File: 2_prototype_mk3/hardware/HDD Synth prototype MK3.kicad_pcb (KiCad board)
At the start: 2 copper layers, 119.4 x 97.4 mm, 60 parts, among them J1 Micro_SD_Card, J3 Bus_ISA_8bit, J4 Conn_01x03, J5 Conn_01x03, Q1 2N3904, SW1 SW_Push, SW2 PEC12R-2120F-S0012, U1 Optocoupler_DC_PhotoNPN_AKEC, U5 MAX98357A, U6 74LS573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

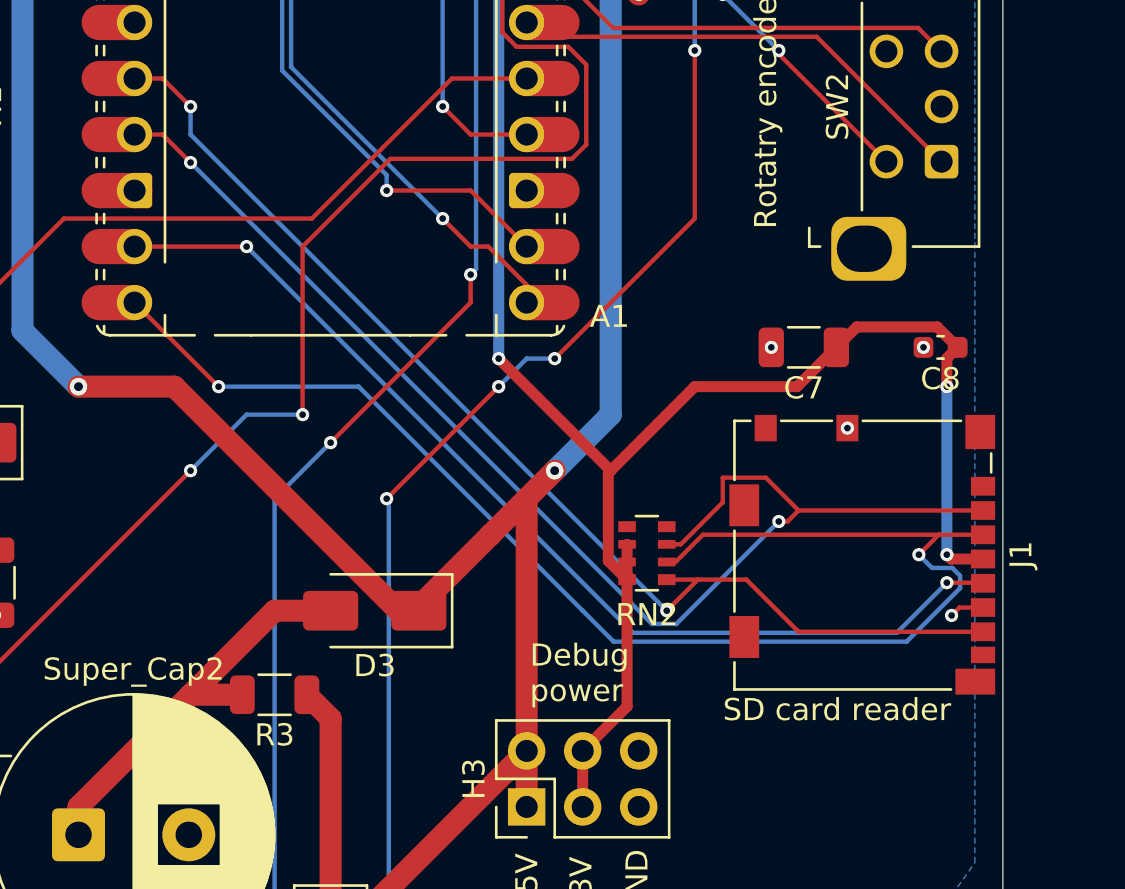
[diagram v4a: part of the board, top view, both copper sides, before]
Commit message: Switch SD card reader to better component
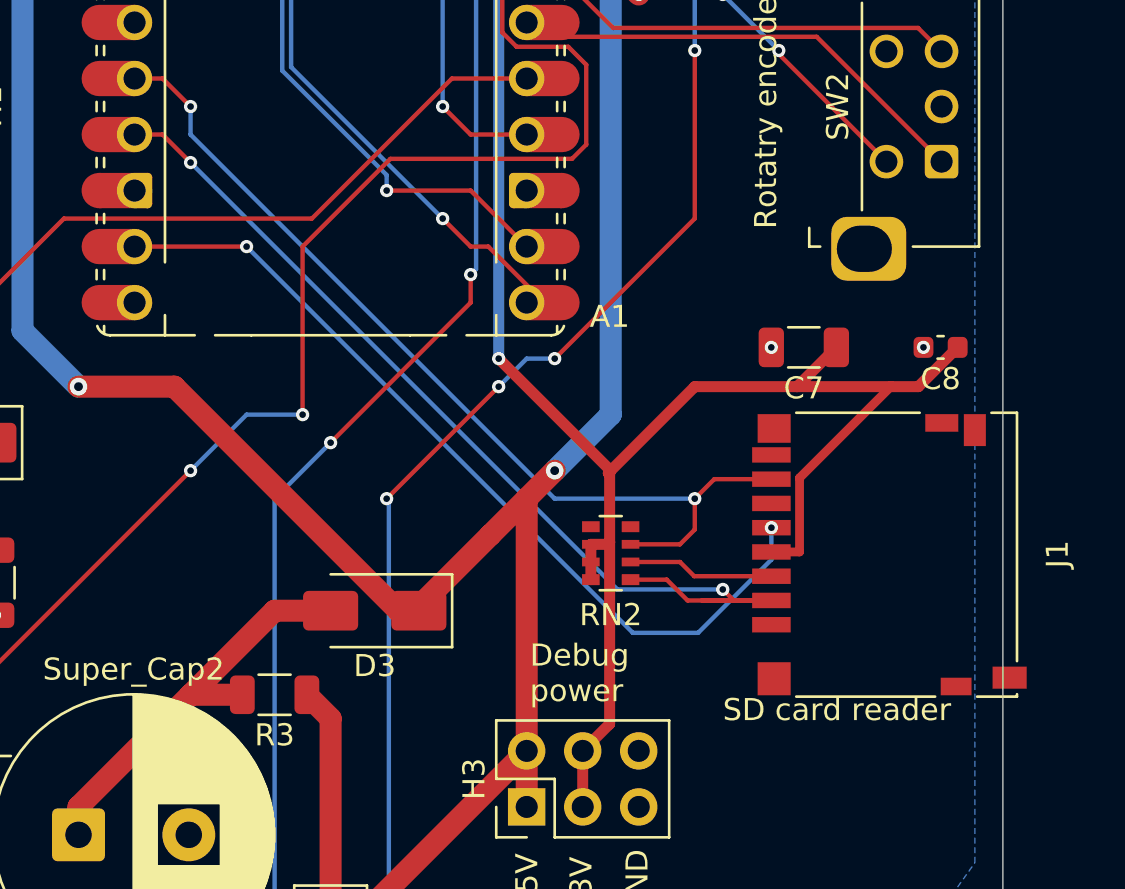
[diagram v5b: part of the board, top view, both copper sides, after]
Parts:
- A1: value RaspberryPi_Pico -> RaspberryPi_Pico2
- J1: footprint Connector_Card:microSD_HC_Molex_104031-0811 -> Connector_Card:microSD_HC_Hirose_DM3D-SF
- moved RN2 1.64 mm to (210.7, 105.3)
- moved J1 1.21 mm to (223.3, 105.4)
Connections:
- RN2 pad 1: /SD_SO -> /SD_CS
- RN2 pad 3: /SD_CS -> /SD_SO
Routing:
- net /SD_SI: track 63.8 -> 6.65 mm, vias 2 -> 0
- net /SD_CS: track 58.3 -> 47.6 mm
- net /SD_SO: track 52.2 -> 42.5 mm
- net /SD_CLK: track 46.7 -> 38.9 mm
- net GND: track 50.6 -> 49.0 mm, vias 28 -> 26
- net +3.3V: track 98.0 -> 99.1 mm, vias 4 -> 2

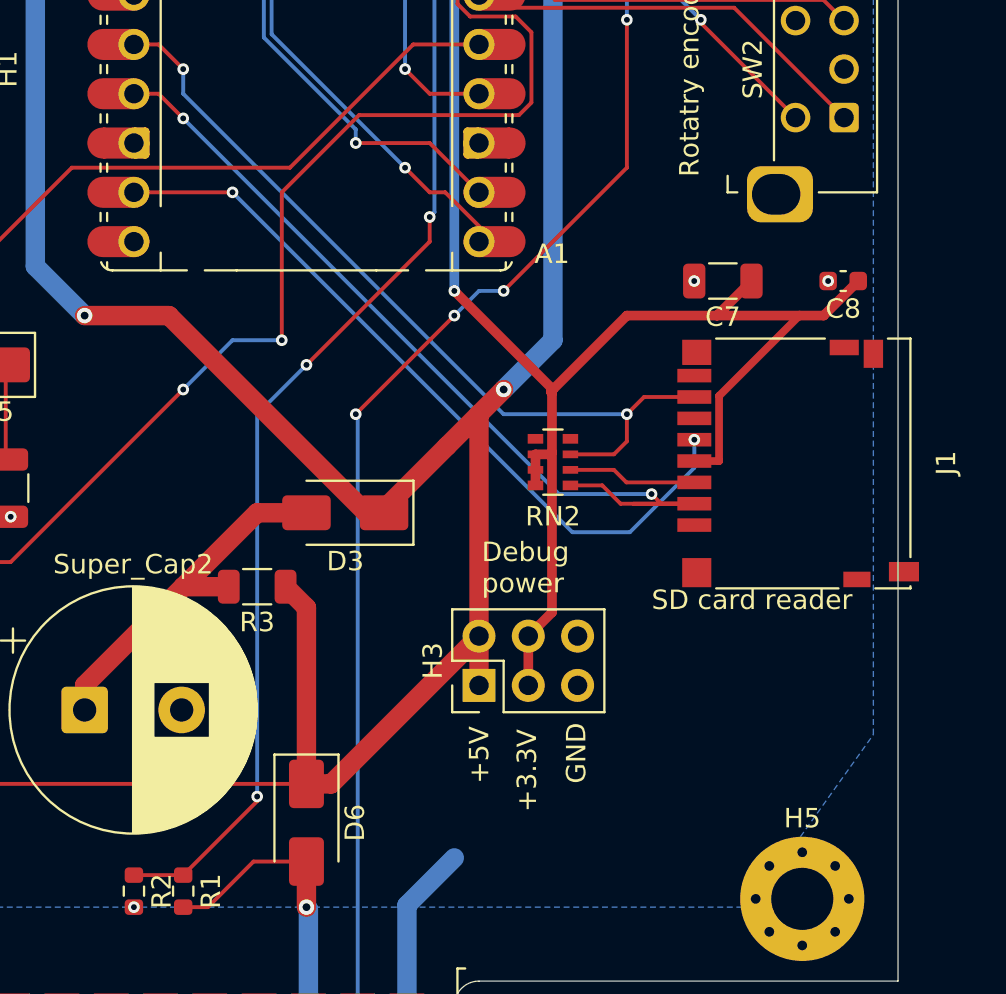
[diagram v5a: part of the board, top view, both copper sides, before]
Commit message: Fix DRC issues and change SD card to injection model
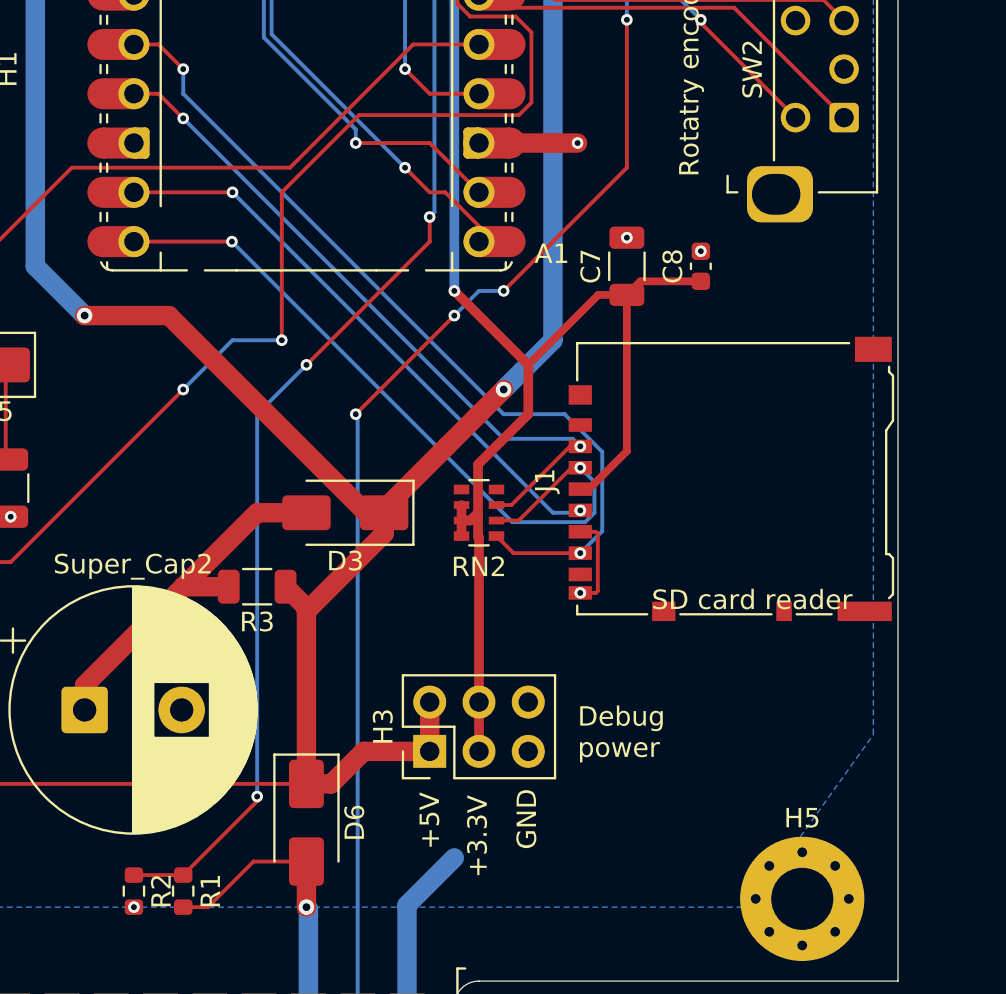
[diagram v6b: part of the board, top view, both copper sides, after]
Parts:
- J1: footprint Connector_Card:microSD_HC_Hirose_DM3D-SF -> Connector_Card:microSD_HC_Hirose_DM3AT-SF-PEJM5
- moved C8 7.37 mm to (218.3, 95.2), turned to 90 degrees
- moved C7 5.00 mm to (214.5, 95.2), turned to 90 degrees
- moved RN2 4.62 mm to (206.9, 107.9)
- moved H3 4.24 mm to (204.3, 120.2)
- moved J1 3.59 mm to (219.8, 106.2), turned to 90 degrees
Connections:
- RN2 pad 1: /SD_CS -> /SD_SO
- RN2 pad 3: /SD_SO -> /SD_CS
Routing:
- net /SD_SI: track 6.65 -> 38.8 mm, vias 0 -> 2
- net /SD_CS: track 47.6 -> 36.1 mm
- net GND: track 49.0 -> 59.0 mm, vias 26 -> 28
- net POWER_5V_SUP: track 295.1 -> 285.4 mm
- net /SD_CLK: track 38.9 -> 29.9 mm
- net +3.3V: track 99.1 -> 93.5 mm
- net /SD_SO: track 42.5 -> 43.9 mm

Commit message: Improve ground connections
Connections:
- J3 pad 10: unconnected-(J3-GND-Pad10) -> GND
- J3 pad 31: unconnected-(J3-GND-Pad31) -> GND
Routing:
- net GND: track 59.0 -> 80.3 mm
- net /ISA IDE activity detection/ISA_A4: track 9.64 -> 11.1 mm

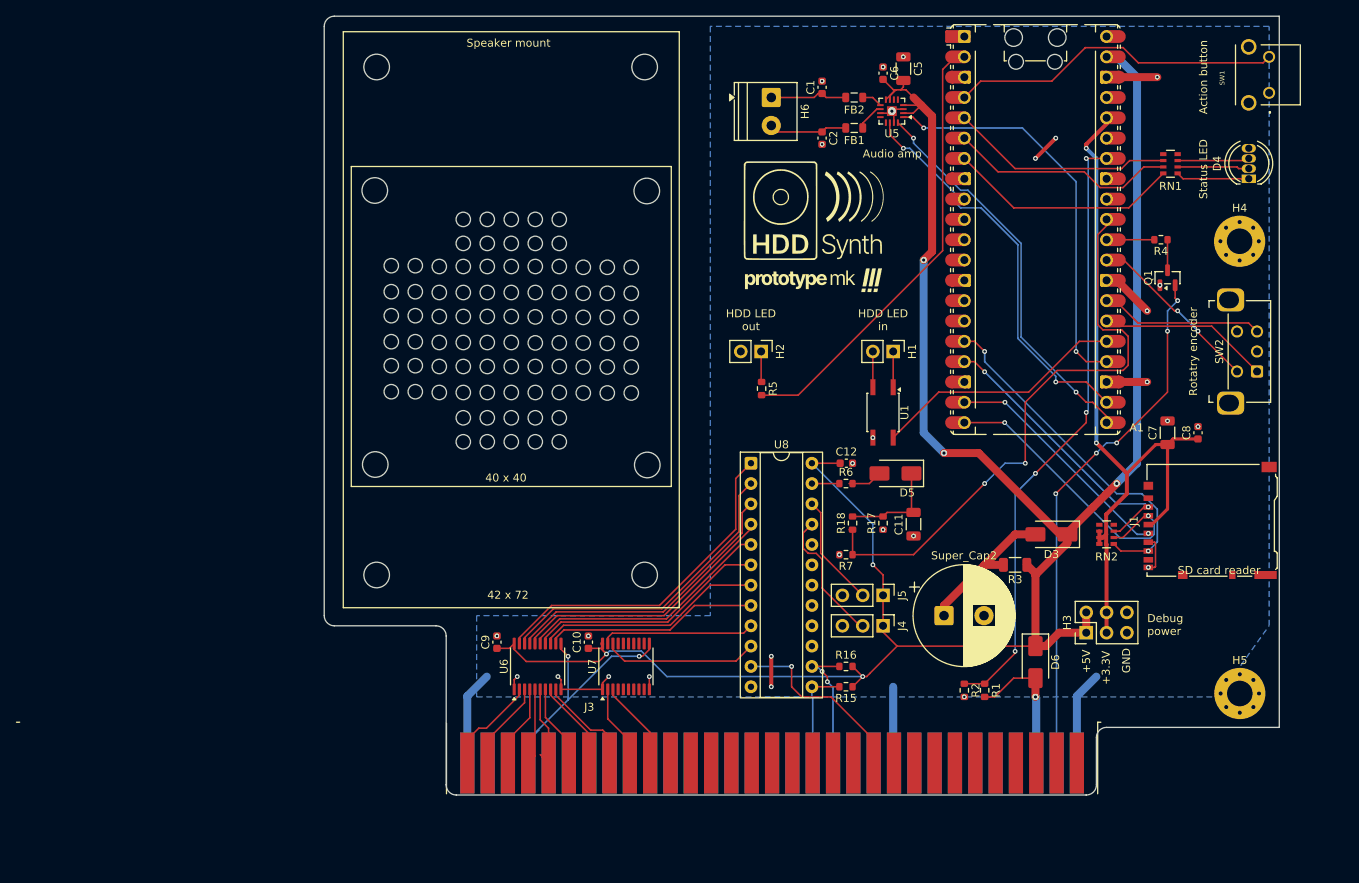
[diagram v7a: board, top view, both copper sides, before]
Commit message: Created FDD connections to Pico and other key components
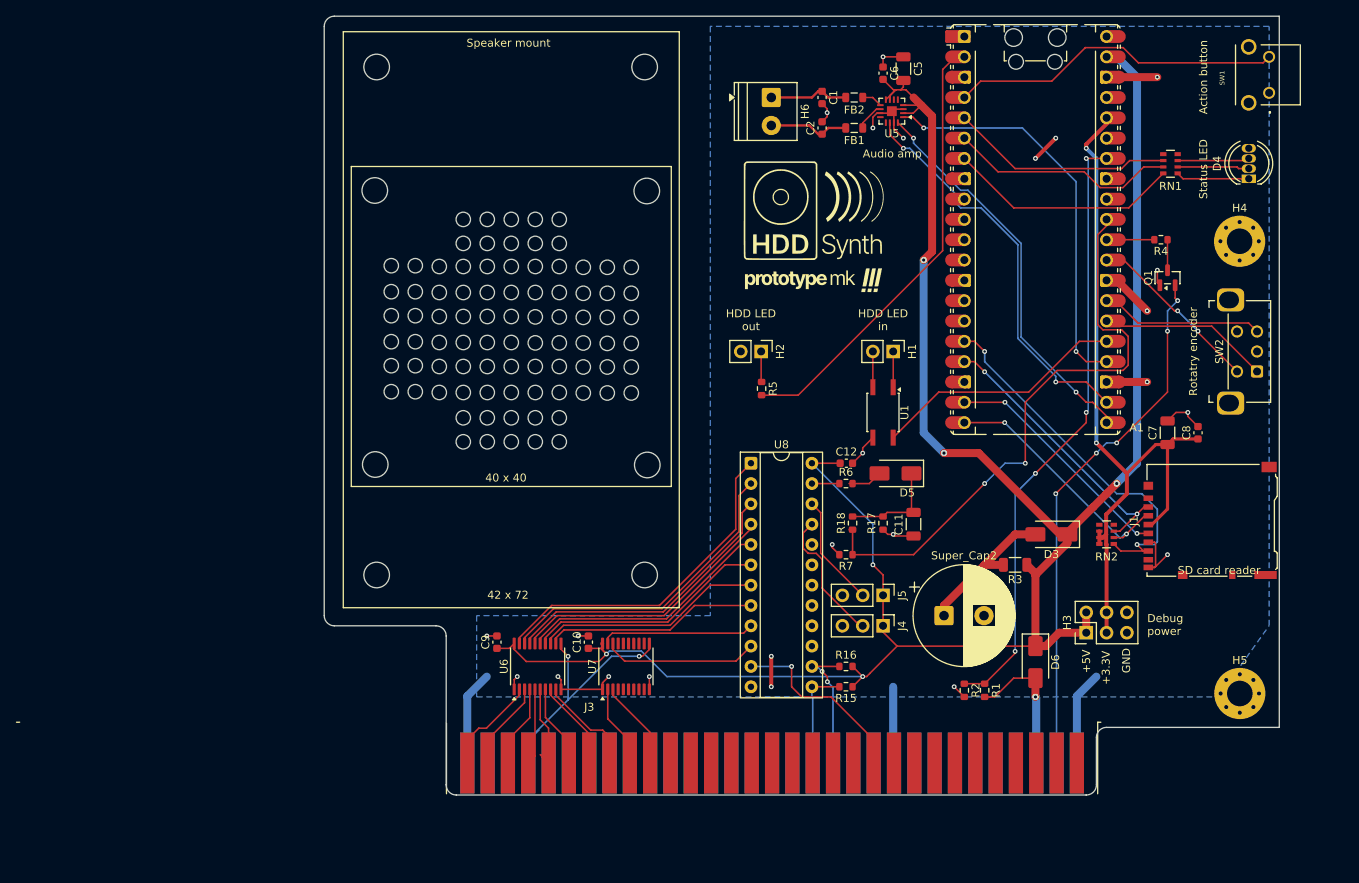
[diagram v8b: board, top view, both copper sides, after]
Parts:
- moved C2 1.27 mm to (171.3, 57.1), turned to 90 degrees
- moved C1 1.27 mm to (171.3, 53.3), turned to -90 degrees
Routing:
- net GND: track 80.3 -> 116.6 mm, vias 28 -> 24
- net /SD_SI: track 38.8 -> 32.7 mm
- net /SD_SO: track 43.9 -> 46.8 mm
- net Net-(H6-Pin_2): track 9.84 -> 11.2 mm
- net /SD_CS: track 36.1 -> 35.1 mm
